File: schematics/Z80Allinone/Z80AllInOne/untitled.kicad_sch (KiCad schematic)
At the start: 9 parts, among them U1 Z80CPU, U2 TC55257CPI, U3 28C256

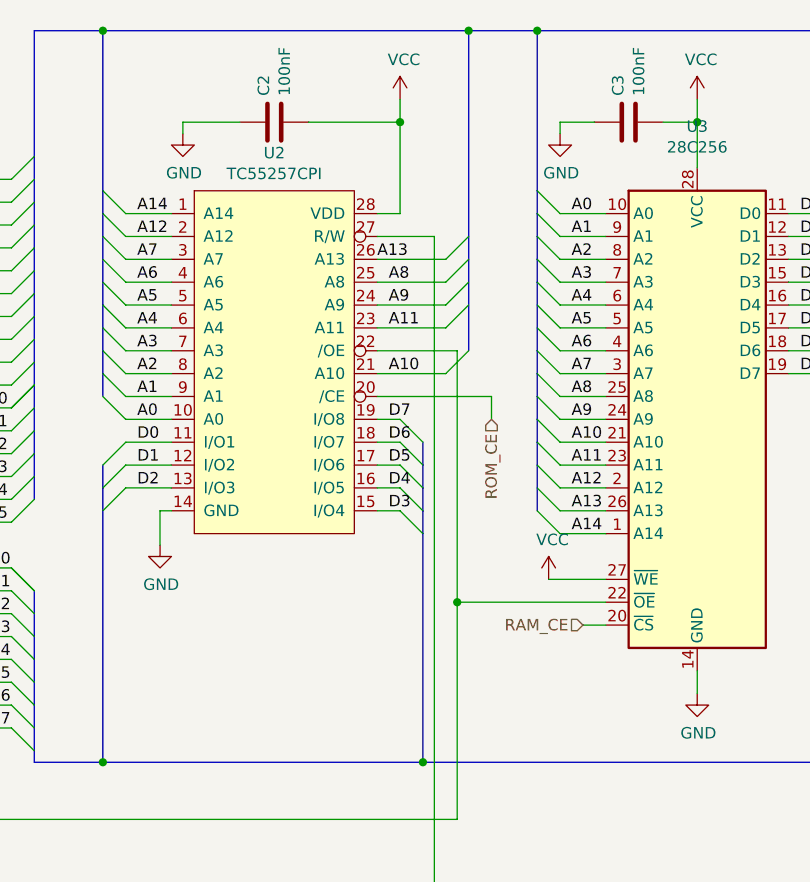
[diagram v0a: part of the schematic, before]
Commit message: Latest changes for adapt source to support Z80AllInOne adding some macros and latest schematic improvements
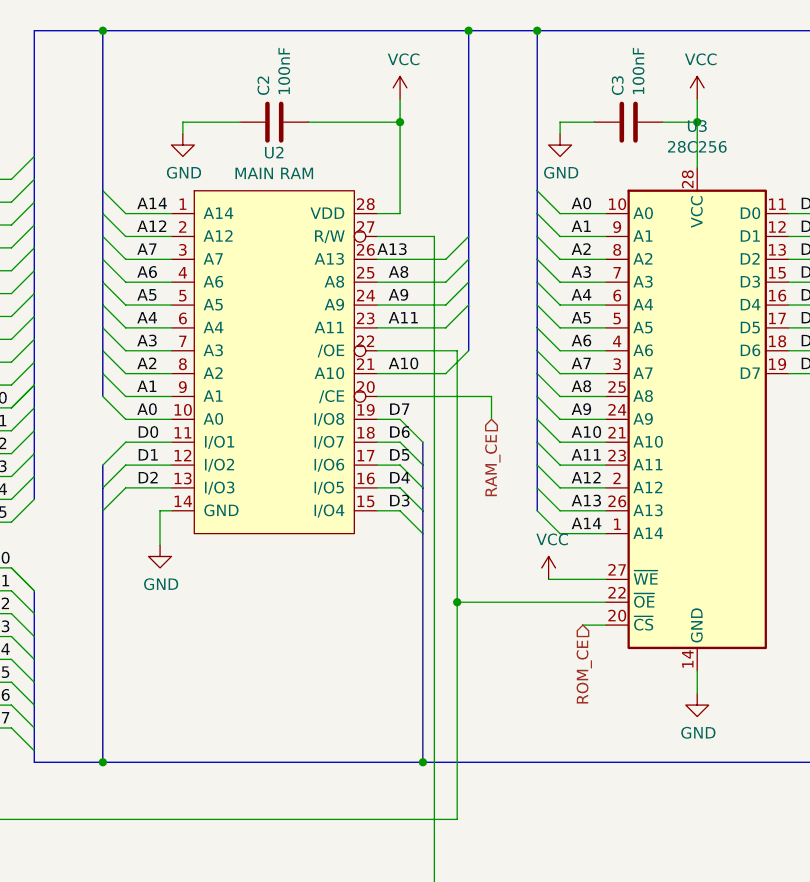
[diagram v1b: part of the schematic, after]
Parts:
- U2: value TC55257CPI -> MAIN RAM
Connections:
- net RAM_CE: now also U2.20 (/CE); no longer U3.20 (~{CS})
- net ROM_CE: now also U3.20 (~{CS}); no longer U2.20 (/CE)
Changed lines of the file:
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@@
-    (effects (font (size 1.27 1.27)) (justify right))
-  )
-  (hierarchical_label "ROM_CE" (shape input) (at 185.42 90.17 270)
     (effects (font (size 1.27 1.27)) (justify right))
   )
@@
     (effects (font (size 1.27 1.27)) (justify right))
   )
-  (hierarchical_label "RAM_CE" (shape input) (at 195.58 113.03 180)
+  (hierarchical_label "RAM_CE" (shape input) (at 185.42 90.17 270)
     (effects (font (size 1.27 1.27)) (justify right))
   )
   (hierarchical_label "GND" (shape input) (at 31.75 31.75 180)
+    (effects (font (size 1.27 1.27)) (justify right))
+  )
+  (hierarchical_label "ROM_CE" (shape input) (at 195.58 113.03 270)
     (effects (font (size 1.27 1.27)) (justify right))
   )
@@
     (in_bom yes) (on_board yes)
     (property "Reference" "U2" (id 0) (at 161.29 60.579 0))
-    (property "Value" "TC55257CPI" (id 1) (at 161.29 62.8904 0))
+    (property "Value" "MAIN RAM" (id 1) (at 161.29 62.8904 0))
     (property "Footprint" "Package_DIP:DIP-28_W15.24mm_LongPads" (id 2) (at 161.29 62.9158 0)
       (effects (font (size 1.27 1.27)) hide)

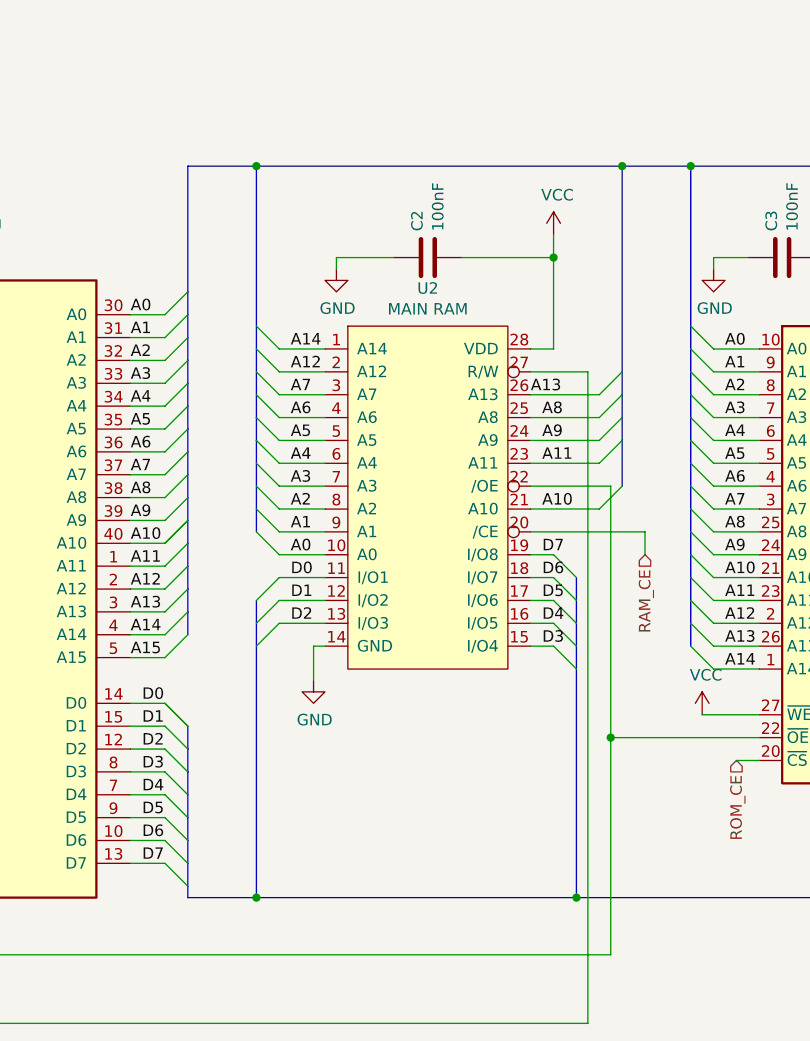
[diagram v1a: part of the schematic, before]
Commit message: Latest changes and replace CTC for 8253 PIT
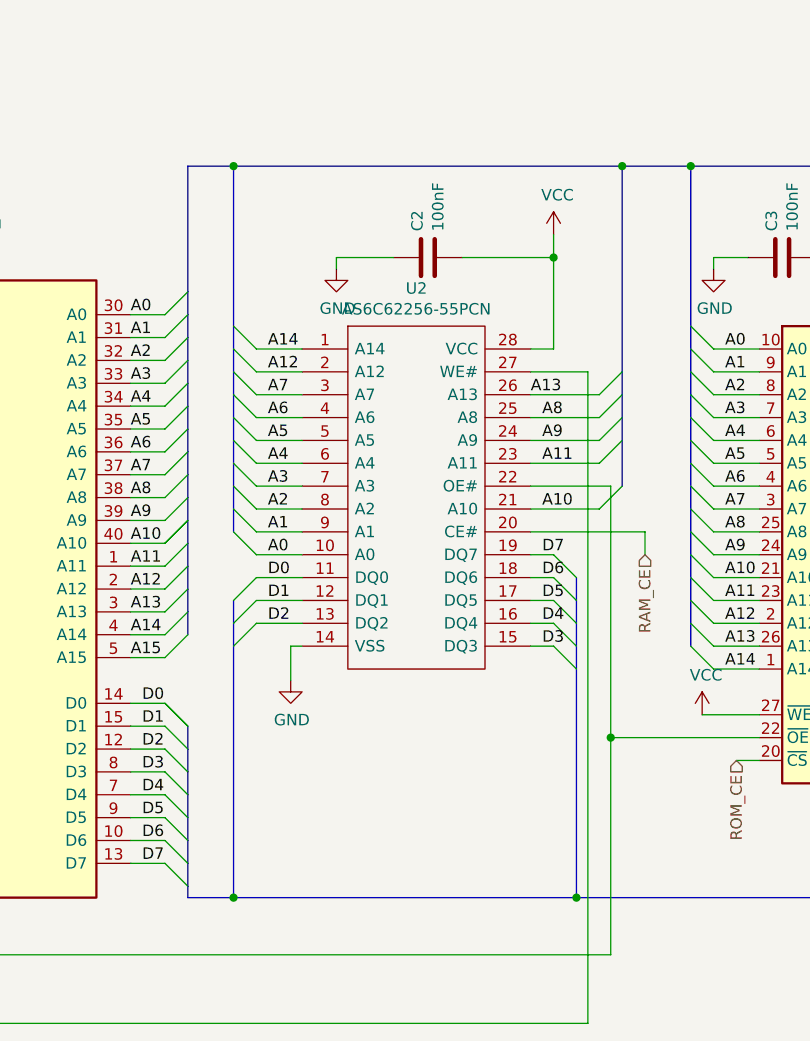
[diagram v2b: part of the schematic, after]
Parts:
- removed U2: MAIN RAM, Package_DIP:DIP-28_W15.24mm_LongPads, symbol Z80Mini-rescue:TC55257CPI-Memory_RAM
- added U2: AS6C62256-55PCN, Package_DIP:DIP-28_W15.24mm_LongPads, symbol Z80MiniFrame-Sound_Graphics-rescue:AS6C62256-55PCN-Memory_RAM
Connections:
- net A0: now also U2.10 (A0)
- net A1: now also U2.9 (A1)
- net A10: now also U2.21 (A10)
- net A11: now also U2.23 (A11)
- net A12: now also U2.2 (A12)
- net A13: now also U2.26 (A13)
- net A14: now also U2.1 (A14)
- net A2: now also U2.8 (A2)
- net A3: now also U2.7 (A3)
- net A4: now also U2.6 (A4)
- net A5: now also U2.5 (A5)
- net A6: now also U2.4 (A6)
- net A7: now also U2.3 (A7)
- net A8: now also U2.25 (A8)
- net A9: now also U2.24 (A9)
- net D0: now also U2.11 (DQ0)
- net D1: now also U2.12 (DQ1)
- net D2: now also U2.13 (DQ2)
- net D3: now also U2.15 (DQ3)
- net D4: now also U2.16 (DQ4)
- net D5: now also U2.17 (DQ5)
- net D6: now also U2.18 (DQ6)
- net D7: now also U2.19 (DQ7)
- net GND: now also U2.14 (VSS)
- net RAM_CE: now also U2.20 (CE#)
- net RD: now also U2.22 (OE#)
- net VCC: now also U2.28 (VCC)
- net WR: now also U2.27 (WE#)
